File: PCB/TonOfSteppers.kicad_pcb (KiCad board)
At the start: 2 copper layers, 177.1 x 150.6 mm, 78 parts, among them J11 SW, J12 SW, J13 SW, J3 Conn_01x12_Male, J4 Conn_01x12_Male, J5 Conn_01x12_Male, J6 Conn_01x12_Male, J7 Conn_01x12_Male, J8 Conn_01x12_Male, J9 Conn_01x12_Male, Q1 Q_NPN_BCE, Q2 Q_NPN_BCE, Q3 Q_NPN_BCE, Q4 Q_NPN_BCE, Q5 Q_NPN_BCE, Q6 Q_NPN_BCE, Q7 Q_PMOS_DGS, U1 LM2678

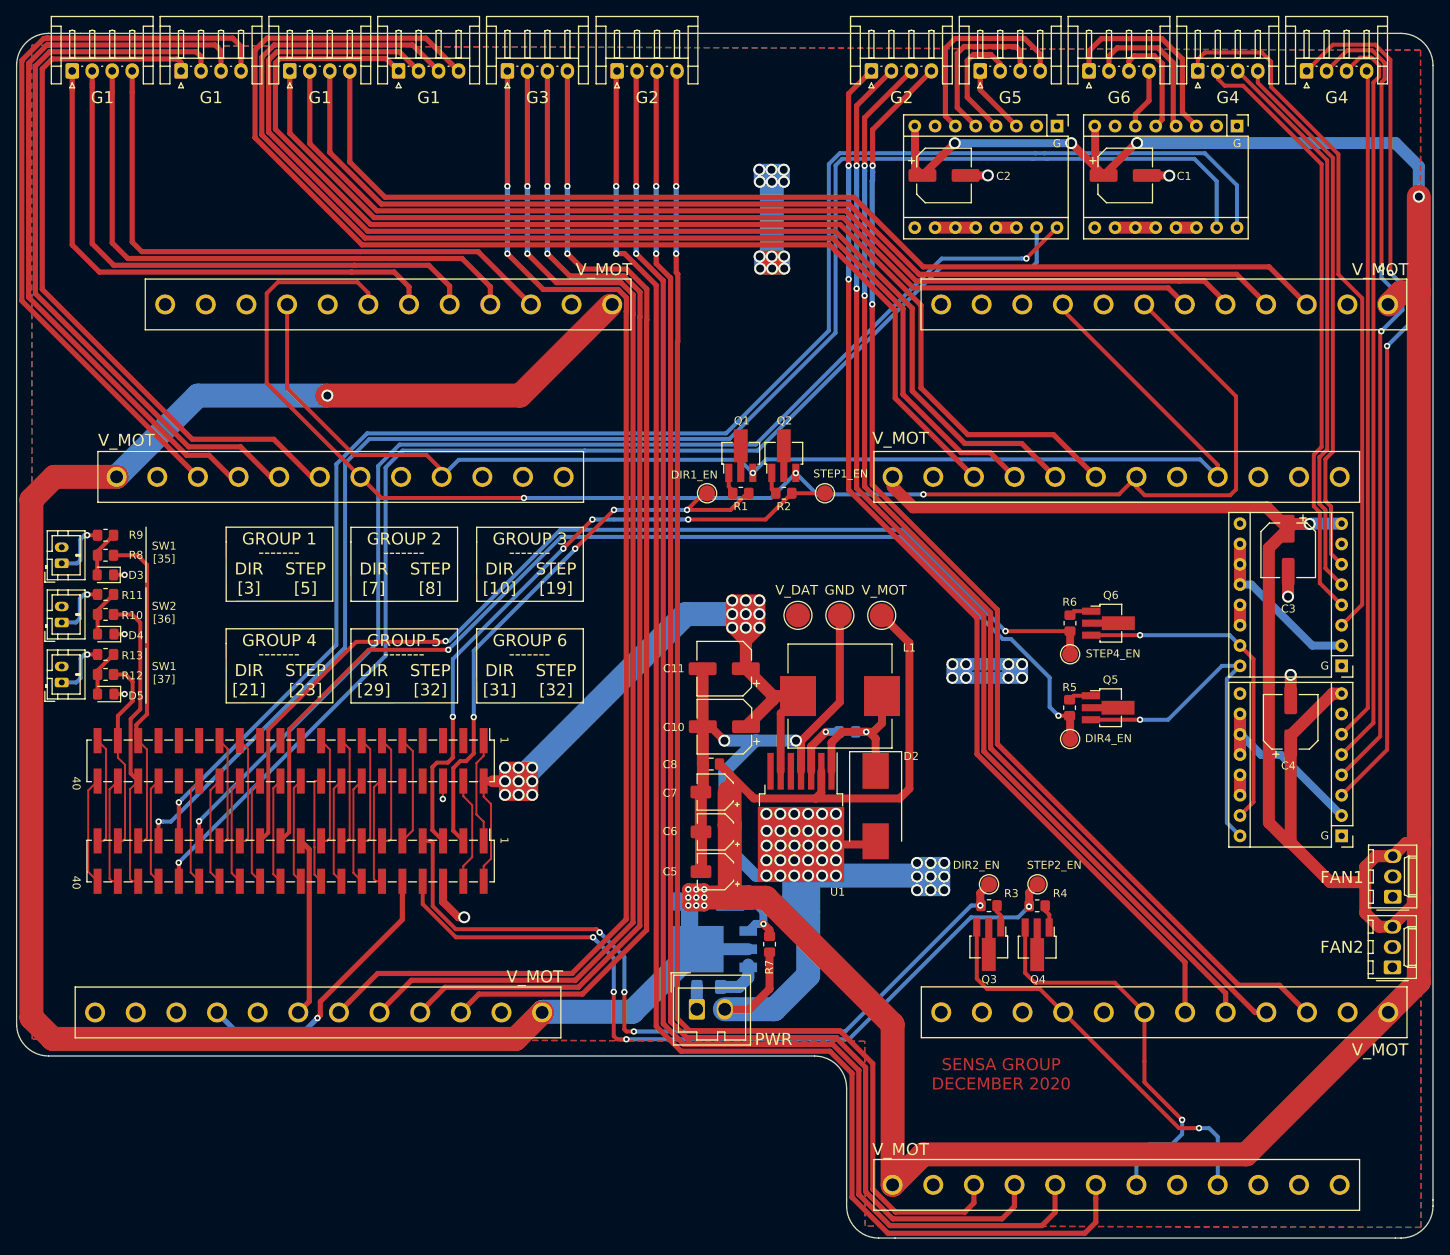
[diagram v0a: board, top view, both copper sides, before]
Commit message: TOS new version
-Added usb power for display.
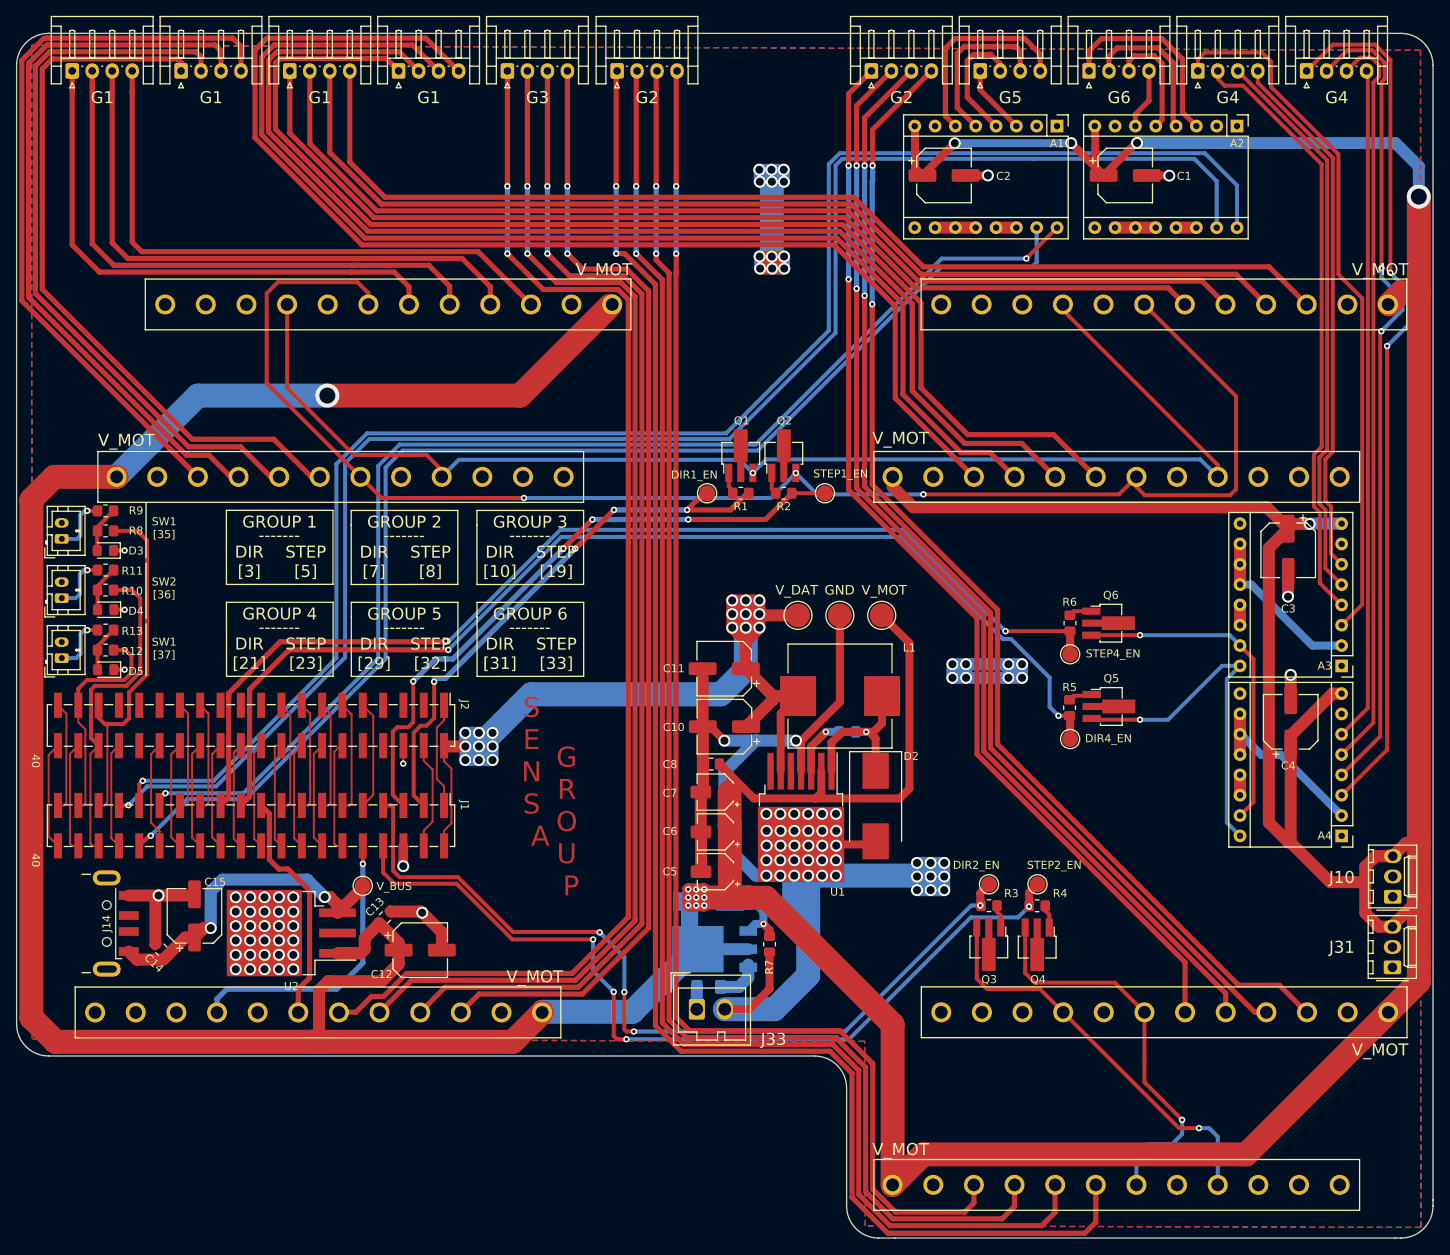
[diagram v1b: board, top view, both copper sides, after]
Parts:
- removed 1: PI To Board, Connector_PinHeader_2.54mm:PinHeader_2x20_P2.54mm_Vertical_SMD
- removed 1: PiGPIO, Connector_PinHeader_2.54mm:PinHeader_2x20_P2.54mm_Vertical_SMD
- added C12: 100uf, Capacitor_SMD:CP_Elec_6.3x7.7, F.Cu at (63.5, 129.5)
- added C13: 0.01uf, Capacitor_SMD:C_0805_2012Metric_Pad1.18x1.45mm_HandSolder, F.Cu at (59.1, 125.4)
- added C14: 0.01uf, Capacitor_SMD:C_0805_2012Metric_Pad1.18x1.45mm_HandSolder, F.Cu at (31.2, 129.5)
- added C15: 100uf, Capacitor_SMD:CP_Elec_6.3x7.7, F.Cu at (35.3, 125.2)
- added J1: PI To Board, Connector_PinHeader_2.54mm:PinHeader_2x20_P2.54mm_Vertical_SMD, F.Cu at (42.4, 114.0)
- added J14: USB_A, Connector_USB:USB_A_CNCTech_1001-011-01101_Horizontal, F.Cu at (17.4, 126.2)
- added J2: PiGPIO, Connector_PinHeader_2.54mm:PinHeader_2x20_P2.54mm_Vertical_SMD, F.Cu at (42.4, 101.4)
- added U2: uA7805, Package_TO_SOT_SMD:TO-263-3_TabPin2, F.Cu at (47.4, 127.4)
- added V_BUS: TestPoint_Pad_D2.0mm, TestPoint:TestPoint_Pad_D2.0mm, F.Cu at (56.3, 121.5)
- moved D3 3.05 mm to (24.2, 79.6)
- moved D4 3.05 mm to (24.2, 87.0)
- moved D5 3.05 mm to (24.2, 94.5)
- moved J11 3.05 mm to (18.7, 78.1)
- moved J12 3.05 mm to (18.7, 85.5)
- moved J13 3.05 mm to (18.7, 93.0)
- moved R10 3.05 mm to (24.2, 84.5)
- moved R11 3.05 mm to (24.2, 82.0)
- moved R12 3.05 mm to (24.2, 92.0)
- moved R13 3.05 mm to (24.2, 89.5)
- moved R8 3.05 mm to (24.2, 77.1)
- moved R9 3.05 mm to (24.2, 74.6)
- moved Q5 0.18 mm to (149.6, 99.1)
- renumbered G to A1, G to A2, G to A3, G to A4, FAN1 to J10, FAN2 to J31, PWR to J33
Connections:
- Q7 pad 1: Net-(D1-Pad2) -> Net-(F1-Pad2)
- Q7 pad 2: V_MOT -> Net-(D1-Pad2)
- Q7 pad 3: Net-(F1-Pad2) -> V_MOT
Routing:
- net GND: track 314.0 -> 422.9 mm, vias 50 -> 82
- net V_BUS: track 0.00 -> 40.3 mm, vias 0 -> 2
- net V_MOT: track 826.7 -> 865.6 mm
- net /STEP3: track 22.5 -> 31.6 mm
- net /Group 2/STEP2_EN: track 101.3 -> 108.3 mm
- net /Group 2/DIR2_EN: track 99.3 -> 106.1 mm
- net 37: track 24.5 -> 29.1 mm
- net 35: track 41.1 -> 45.3 mm
- net /Group 4/STEP4_EN: track 133.0 -> 136.6 mm
- net /Group 4/DIR4_EN: track 136.3 -> 139.7 mm
- net /DIR5: track 153.4 -> 156.7 mm
- net 36: track 38.3 -> 41.3 mm
- net /DIR6: track 203.1 -> 205.9 mm
- net /STEP6: track 201.7 -> 204.2 mm
- net /STEP5: track 158.8 -> 160.8 mm
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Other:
- board text added: "G R O U P"
- board text added: "S E N S A"
- board text added: "STEP [33]"
- board text removed: "SENSA GROUP DECEMBER 2020"
